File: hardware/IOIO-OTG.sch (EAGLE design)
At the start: 58 parts, among them Q1 IRLML2244, Q2 2N7002PW, Q3 AO3404A, U1 PIC24FJ256GB206, U14 SWITCH_SPDT, U2 TPS62133RGTT, U3 VREG_MIC5216

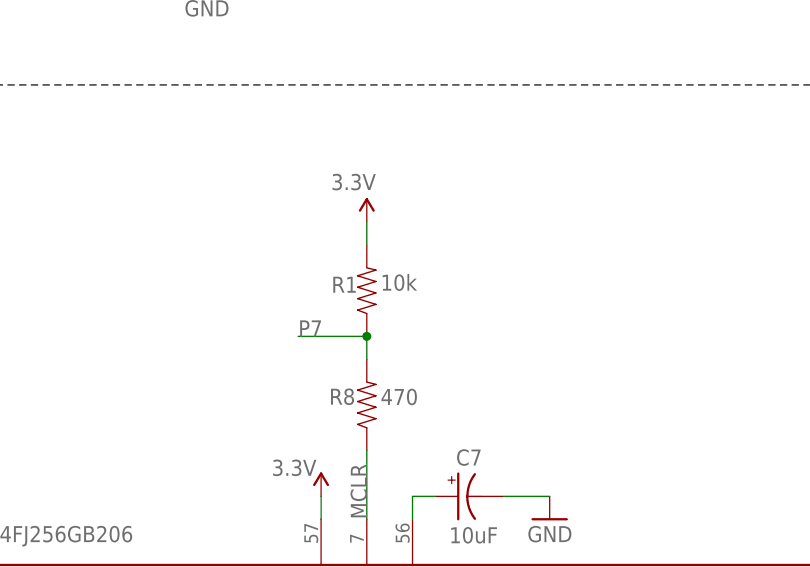
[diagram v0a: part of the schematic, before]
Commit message: Moved R1, R8, C4 to proper 0603 packages
All three components had to move slightly. This will require updating
their x/y coordinates.
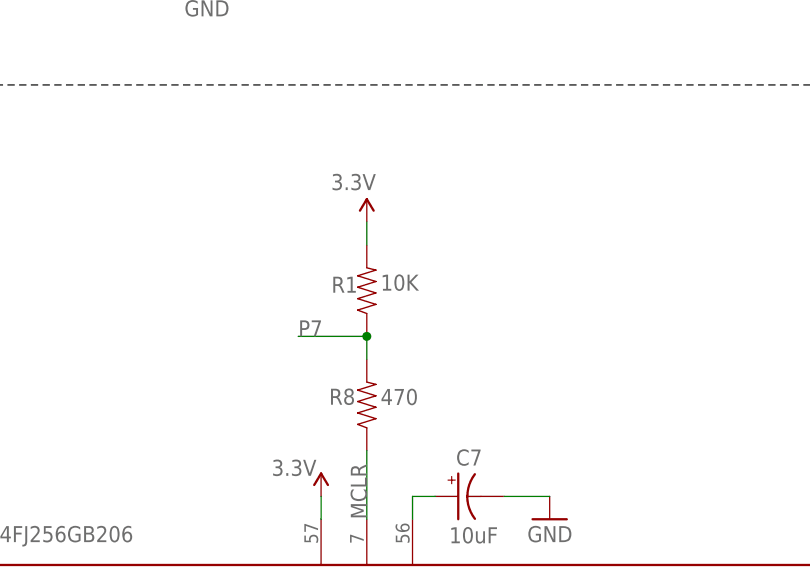
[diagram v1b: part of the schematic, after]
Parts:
- C4: device SparkFun:CAP0402-CAP -> SparkFun-Capacitors:0.1UF-25V(+80/-20%)(0603)
- R1: value 10k -> 10K; device SparkFun:RESISTOR0402-RES -> SparkFun-Resistors:10KOHM-1/10W-1%(0603)0603
- R8: device SparkFun:RESISTOR0402-RES -> SparkFun-Resistors:470OHM1/10W1%(0603)
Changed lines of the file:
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@@
 <grid distance="0.1" unitdist="inch" unit="inch" style="lines" multiple="1" display="no" altdistance="0.01" altunitdist="inch" altunit="inch"/>
 <layers>
-<layer number="1" name="Top" color="4" fill="1" visible="yes" active="no"/>
-<layer number="2" name="Route2" color="1" fill="3" visible="yes" active="no"/>
-<layer number="3" name="Route3" color="4" fill="3" visible="yes" active="no"/>
-<layer number="4" name="Route4" color="1" fill="4" visible="yes" active="no"/>
-<layer number="5" name="Route5" color="4" fill="4" visible="yes" active="no"/>
-<layer number="6" name="Route6" color="1" fill="8" visible="yes" active="no"/>
-<layer number="7" name="Route7" color="4" fill="8" visible="yes" active="no"/>
-<layer number="8" name="Route8" color="1" fill="2" visible="yes" active="no"/>
-<layer number="9" name="Route9" color="4" fill="2" visible="yes" active="no"/>
-<layer number="10" name="Route10" color="1" fill="7" visible="yes" active="no"/>
-<layer number="11" name="Route11" color="4" fill="7" visible="yes" active="no"/>
-<layer number="12" name="Route12" color="1" fill="5" visible="yes" active="no"/>
-<layer number="13" name="Route13" color="4" fill="5" visible="yes" active="no"/>
-<layer number="14" name="Route14" color="1" fill="6" visible="yes" active="no"/>
-<layer number="15" name="Route15" color="4" fill="6" visible="yes" active="no"/>
-<layer number="16" name="Bottom" color="1" fill="1" visible="yes" active="no"/>
-<layer number="17" name="Pads" color="2" fill="1" visible="yes" active="no"/>
-<layer number="18" name="Vias" color="2" fill="1" visible="yes" active="no"/>
-<layer number="19" name="Unrouted" color="6" fill="1" visible="yes" active="no"/>
-<layer number="20" name="Dimension" color="15" fill="1" visible="yes" active="no"/>
-<layer number="21" name="tPlace" color="16" fill="1" visible="yes" active="no"/>
-<layer number="22" name="bPlace" color="14" fill="1" visible="yes" active="no"/>
-<layer number="23" name="tOrigins" color="15" fill="1" visible="yes" active="no"/>
-<layer number="24" name="bOrigins" color="15" fill="1" visible="yes" active="no"/>
-<layer number="25" name="tNames" color="7" fill="1" visible="yes" active="no"/>
-<layer number="26" name="bNames" color="3" fill="1" visible="yes" active="no"/>
-<layer number="27" name="tValues" color="7" fill="1" visible="yes" active="no"/>
-<layer number="28" name="bValues" color="7" fill="1" visible="yes" active="no"/>
+<layer number="1" name="Top" color="4" fill="1" visible="no" active="no"/>
+<layer number="2" name="Route2" color="1" fill="3" visible="no" active="no"/>
+<layer number="3" name="Route3" color="4" fill="3" visible="no" active="no"/>
+<layer number="4" name="Route4" color="1" fill="4" visible="no" active="no"/>
+<layer number="5" name="Route5" color="4" fill="4" visible="no" active="no"/>
+<layer number="6" name="Route6" color="1" fill="8" visible="no" active="no"/>
+<layer number="7" name="Route7" color="4" fill="8" visible="no" active="no"/>
+<layer number="8" name="Route8" color="1" fill="2" visible="no" active="no"/>
+<layer number="9" name="Route9" color="4" fill="2" visible="no" active="no"/>
+<layer number="10" name="Route10" color="1" fill="7" visible="no" active="no"/>
+<layer number="11" name="Route11" color="4" fill="7" visible="no" active="no"/>
+<layer number="12" name="Route12" color="1" fill="5" visible="no" active="no"/>
+<layer number="13" name="Route13" color="4" fill="5" visible="no" active="no"/>
+<layer number="14" name="Route14" color="1" fill="6" visible="no" active="no"/>
+<layer number="15" name="Route15" color="4" fill="6" visible="no" active="no"/>
+<layer number="16" name="Bottom" color="1" fill="1" visible="no" active="no"/>
+<layer number="17" name="Pads" color="2" fill="1" visible="no" active="no"/>
+<layer number="18" name="Vias" color="2" fill="1" visible="no" active="no"/>
+<layer number="19" name="Unrouted" color="6" fill="1" visible="no" active="no"/>
+<layer number="20" name="Dimension" color="15" fill="1" visible="no" active="no"/>
+<layer number="21" name="tPlace" color="16" fill="1" visible="no" active="no"/>
+<layer number="22" name="bPlace" color="14" fill="1" visible="no" active="no"/>
+<layer number="23" name="tOrigins" color="15" fill="1" visible="no" active="no"/>
+<layer number="24" name="bOrigins" color="15" fill="1" visible="no" active="no"/>
+<layer number="25" name="tNames" color="7" fill="1" visible="no" active="no"/>
+<layer number="26" name="bNames" color="3" fill="1" visible="no" active="no"/>
+<layer number="27" name="tValues" color="7" fill="1" visible="no" active="no"/>
+<layer number="28" name="bValues" color="7" fill="1" visible="no" active="no"/>
 <layer number="29" name="tStop" color="7" fill="3" visible="no" active="no"/>
 <layer number="30" name="bStop" color="3" fill="6" visible="no" active="no"/>
@@
 <layer number="35" name="tGlue" color="7" fill="4" visible="no" active="no"/>
 <layer number="36" name="bGlue" color="3" fill="5" visible="no" active="no"/>
-<layer number="37" name="tTest" color="7" fill="1" visible="yes" active="no"/>
-<layer number="38" name="bTest" color="3" fill="1" visible="yes" active="no"/>
+<layer number="37" name="tTest" color="7" fill="1" visible="no" active="no"/>
+<layer number="38" name="bTest" color="3" fill="1" visible="no" active="no"/>
 <layer number="39" name="tKeepout" color="4" fill="11" visible="no" active="no"/>
 <layer number="40" name="bKeepout" color="1" fill="11" visible="no" active="no"/>
@@
 <layer number="44" name="Drills" color="7" fill="1" visible="no" active="no"/>
 <layer number="45" name="Holes" color="7" fill="1" visible="no" active="no"/>
-<layer number="46" name="Milling" color="3" fill="1" visible="yes" active="no"/>
-<layer number="47" name="Measures" color="7" fill="1" visible="yes" active="no"/>
-<layer number="48" name="Document" color="7" fill="1" visible="yes" active="no"/>
-<layer number="49" name="Reference" color="7" fill="1" visible="yes" active="no"/>
-<layer number="50" name="dxf" color="7" fill="1" visible="yes" active="no"/>
-<layer number="51" name="tDocu" color="6" fill="1" visible="yes" active="no"/>
-<layer number="52" name="bDocu" color="7" fill="1" visible="yes" active="no"/>
-<layer number="53" name="tGND_GNDA" color="7" fill="9" visible="yes" active="no"/>
-<layer number="54" name="bGND_GNDA" color="1" fill="9" visible="yes" active="no"/>
-<layer number="56" name="wert" color="7" fill="1" visible="yes" active="no"/>
-<layer number="57" name="tCAD" color="7" fill="1" visible="yes" active="no"/>
-<layer number="59" name="tCarbon" color="7" fill="1" visible="yes" active="no"/>
-<layer number="60" name="bCarbon" color="7" fill="1" visible="yes" active="no"/>
+<layer number="46" name="Milling" color="3" fill="1" visible="no" active="no"/>
+<layer number="47" name="Measures" color="7" fill="1" visible="no" active="no"/>
+<layer number="48" name="Document" color="7" fill="1" visible="no" active="no"/>
+<layer number="49" name="Reference" color="7" fill="1" visible="no" active="no"/>
+<layer number="50" name="dxf" color="7" fill="1" visible="no" active="no"/>
+<layer number="51" name="tDocu" color="6" fill="1" visible="no" active="no"/>
+<layer number="52" name="bDocu" color="7" fill="1" visible="no" active="no"/>
+<layer number="53" name="tGND_GNDA" color="7" fill="9" visible="no" active="no"/>
+<layer number="54" name="bGND_GNDA" color="1" fill="9" visible="no" active="no"/>
+<layer number="56" name="wert" color="7" fill="1" visible="no" active="no"/>
+<layer number="57" name="tCAD" color="7" fill="1" visible="no" active="no"/>
+<layer number="59" name="tCarbon" color="7" fill="1" visible="no" active="no"/>
+<layer number="60" name="bCarbon" color="7" fill="1" visible="no" active="no"/>
 <layer number="90" name="Modules" color="5" fill="1" visible="yes" active="yes"/>
 <layer number="91" name="Nets" color="2" fill="1" visible="yes" active="yes"/>
@@
 <part name="C2" library="SparkFun" deviceset="CAP" device="0402-CAP" value="0.1uF"/>
 <part name="C3" library="SparkFun" deviceset="CAP" device="0402-CAP" value="0.1uF"/>
-<part name="C4" library="SparkFun" deviceset="CAP" device="0402-CAP" value="0.1uF"/>
+<part name="C4" library="SparkFun-Capacitors" deviceset="0.1UF-25V(+80/-20%)(0603)" device="" value="0.1uF"/>
 <part name="C7" library="SparkFun" deviceset="CAP_POL" device="1206" value="10uF"/>
 <part name="P+1" library="SparkFun" deviceset="3.3V" device=""/>
@@
 <part name="GND4" library="SparkFun" deviceset="GND" device=""/>
 <part name="GND5" library="SparkFun" deviceset="GND" device=""/>
-<part name="R1" library="SparkFun" deviceset="RESISTOR" device="0402-RES" value="10k"/>
+<part name="R1" library="SparkFun-Resistors" deviceset="10KOHM-1/10W-1%(0603)" device="0603" value="10K"/>
 <part name="P+6" library="SparkFun" deviceset="3.3V" device=""/>
 <part name="C5" library="SparkFun" deviceset="CAP" device="0402-CAP" value="0.1uF"/>
@@
 <part name="R7" library="SparkFun" deviceset="RESISTOR" device="0402-RES" value="750"/>
 <part name="P+11" library="SparkFun" deviceset="3.3V" device=""/>
-<part name="R8" library="SparkFun" deviceset="RESISTOR" device="0402-RES" value="470"/>
+<part name="R8" library="SparkFun-Resistors" deviceset="470OHM1/10W1%(0603)" device="" value="470"/>
 <part name="FRAME1" library="SparkFun" deviceset="FRAME-A3" device=""/>
 <part name="JP10" library="SparkFun" deviceset="STAND-OFF" device=""/>

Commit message: Moved C1 and L1 to proper 0603 packages
moved X/Y coordinates
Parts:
- C1: device SparkFun:CAP0402-CAP -> SparkFun-Capacitors:0.1UF-25V(+80/-20%)(0603)
- L1: device SparkFun-Passives:INDUCTOR0402 -> SparkFun-Passives:INDUCTOR30OHM,1.8A
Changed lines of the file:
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@@
 <parts>
 <part name="U1" library="SparkFun-DigitalIC" deviceset="PIC24FXXXDAX06" device="" value="PIC24FJ256GB206"/>
-<part name="C1" library="SparkFun" deviceset="CAP" device="0402-CAP" value="0.1uF"/>
+<part name="C1" library="SparkFun-Capacitors" deviceset="0.1UF-25V(+80/-20%)(0603)" device="" value="0.1uF"/>
 <part name="C2" library="SparkFun" deviceset="CAP" device="0402-CAP" value="0.1uF"/>
 <part name="C3" library="SparkFun" deviceset="CAP" device="0402-CAP" value="0.1uF"/>
@@
 <attribute name="PART#" value="TS53YL502MR10"/>
 </part>
-<part name="L1" library="SparkFun-Passives" deviceset="INDUCTOR" device="0402" value="30Ohm,1.8A"/>
+<part name="L1" library="SparkFun-Passives" deviceset="INDUCTOR" device="30OHM,1.8A" value="30Ohm,1.8A"/>
 <part name="U14" library="SparkFun-Electromechanical" deviceset="SWITCH_SPDT" device=""/>
 <part name="JP9" library="SparkFun-Connectors" deviceset="M11" device="1X11_NO_SILK"/>

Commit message: Moved C3 to proper 0603 package
moved X/Y coordinate
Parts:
- C3: device SparkFun:CAP0402-CAP -> SparkFun-Capacitors:0.1UF-25V(+80/-20%)(0603)
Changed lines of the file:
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@@
 <part name="C1" library="SparkFun-Capacitors" deviceset="0.1UF-25V(+80/-20%)(0603)" device="" value="0.1uF"/>
 <part name="C2" library="SparkFun" deviceset="CAP" device="0402-CAP" value="0.1uF"/>
-<part name="C3" library="SparkFun" deviceset="CAP" device="0402-CAP" value="0.1uF"/>
+<part name="C3" library="SparkFun-Capacitors" deviceset="0.1UF-25V(+80/-20%)(0603)" device="" value="0.1uF"/>
 <part name="C4" library="SparkFun-Capacitors" deviceset="0.1UF-25V(+80/-20%)(0603)" device="" value="0.1uF"/>
 <part name="C7" library="SparkFun" deviceset="CAP_POL" device="1206" value="10uF"/>
